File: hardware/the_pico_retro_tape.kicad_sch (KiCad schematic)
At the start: 1 part, among them U1 Pico

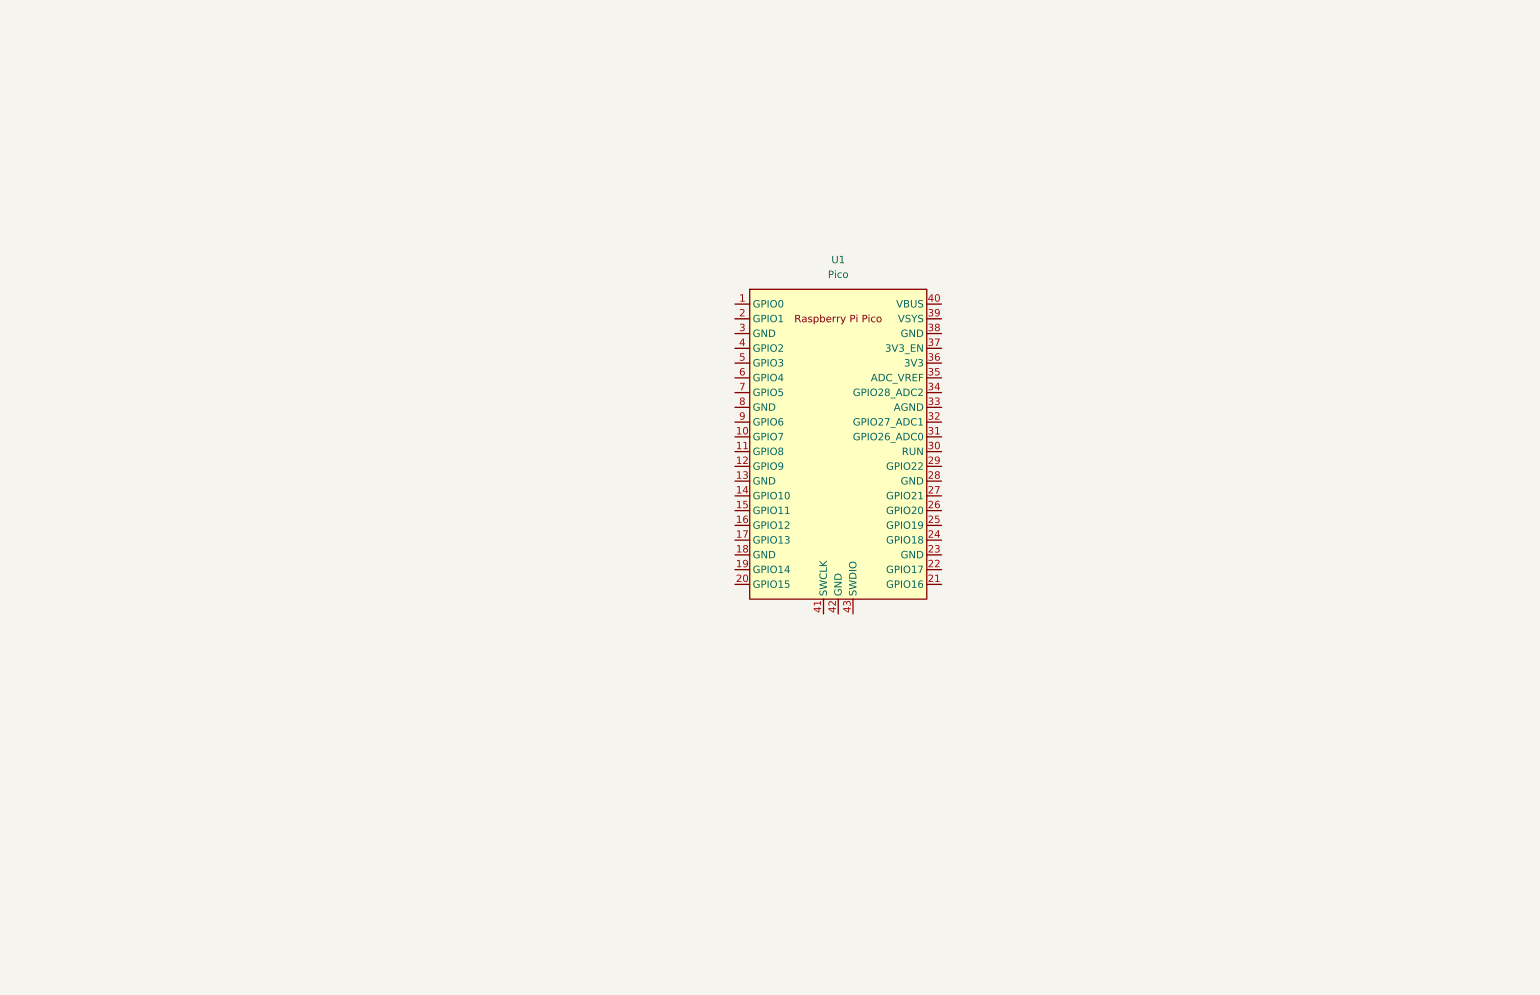
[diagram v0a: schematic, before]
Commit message: update schematic
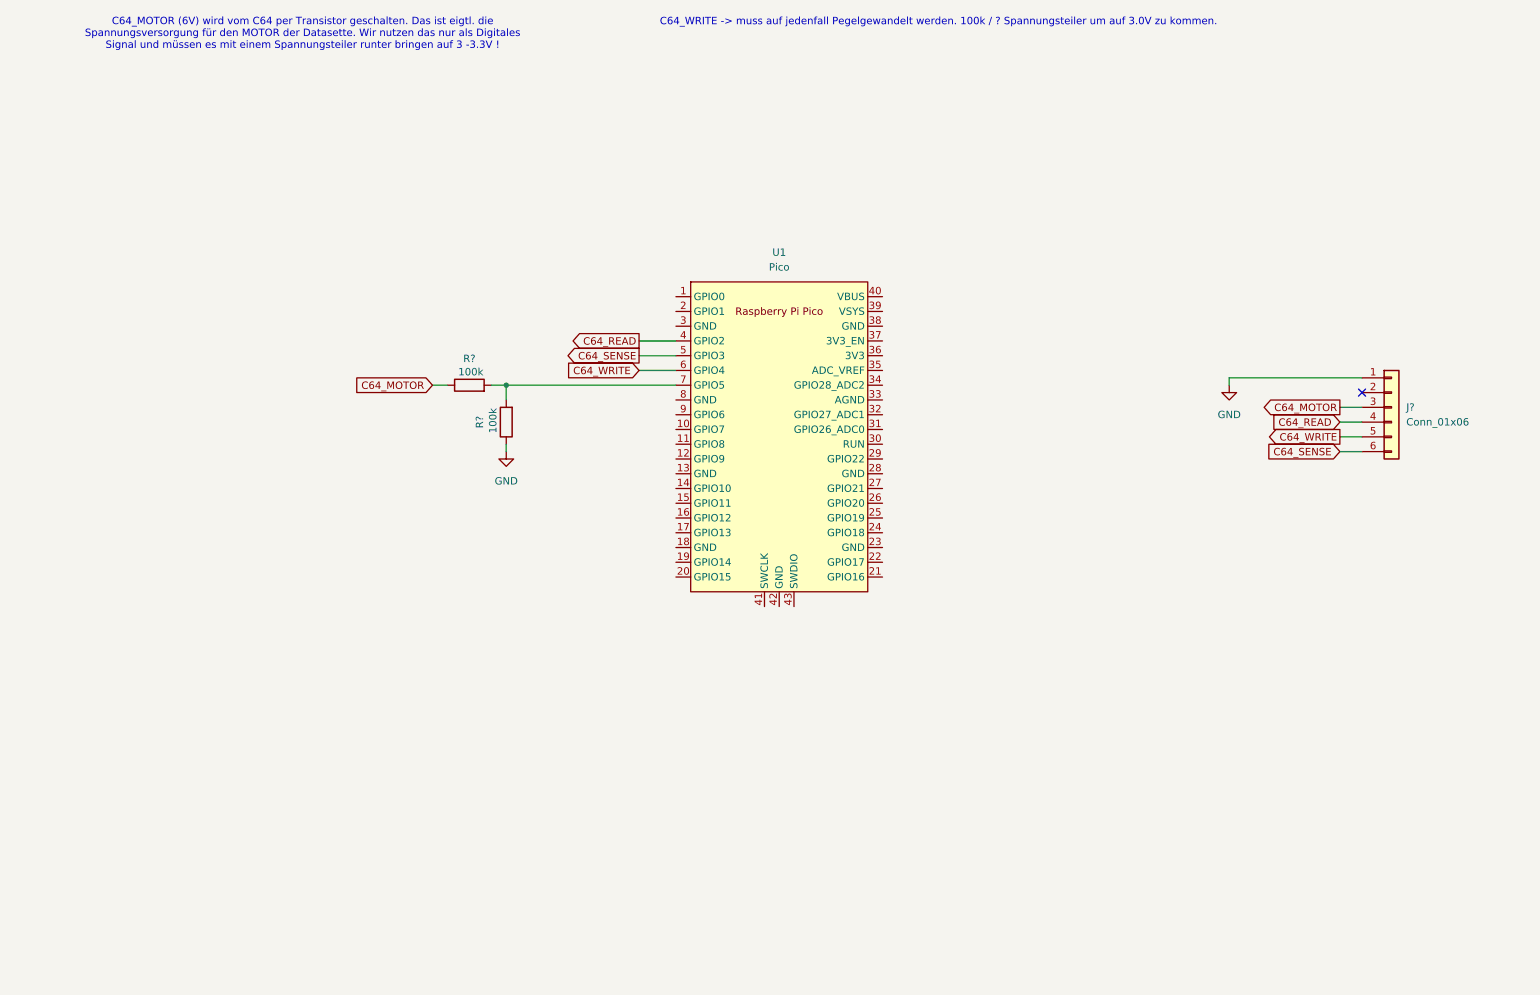
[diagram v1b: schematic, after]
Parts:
- added J?: Conn_01x06, symbol Connector_Generic:Conn_01x06
- added R? (x2): 100k, symbol Device:R
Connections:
- net C64_READ: now reaches U1.4 (GPIO2)
- net C64_READ: now also J?.4 (Pin_4)
- net C64_SENSE: now reaches U1.5 (GPIO3)
- net C64_SENSE: now also J?.6 (Pin_6)
- net C64_WRITE: now reaches U1.6 (GPIO4)
- net C64_WRITE: now also J?.5 (Pin_5)
- net at U1.7 (GPIO5): now also R?.2, R?.2
- new net C64_MOTOR: J?.3 (Pin_3), R?.1
- new net GND: J?.1 (Pin_1), R?.1
- no-connect marks 0 -> 1
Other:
- note added: "C64_MOTOR (6V) wird vom C64 per Transistor geschalten. Das ist eigtl. die Spannungsversorgung für den MOTOR der Datasette. Wir nutzen das nur als Digitales Signal und müssen es mit einem Spannungsteiler runter bringen auf 3 -3.3V !"
- note added: "C64_WRITE -> muss auf jedenfall Pegelgewandelt werden. 100k / ? Spannungsteiler um auf 3.0V zu kommen."
- moved on the sheet: U1

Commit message: schematic: added the sd card modul
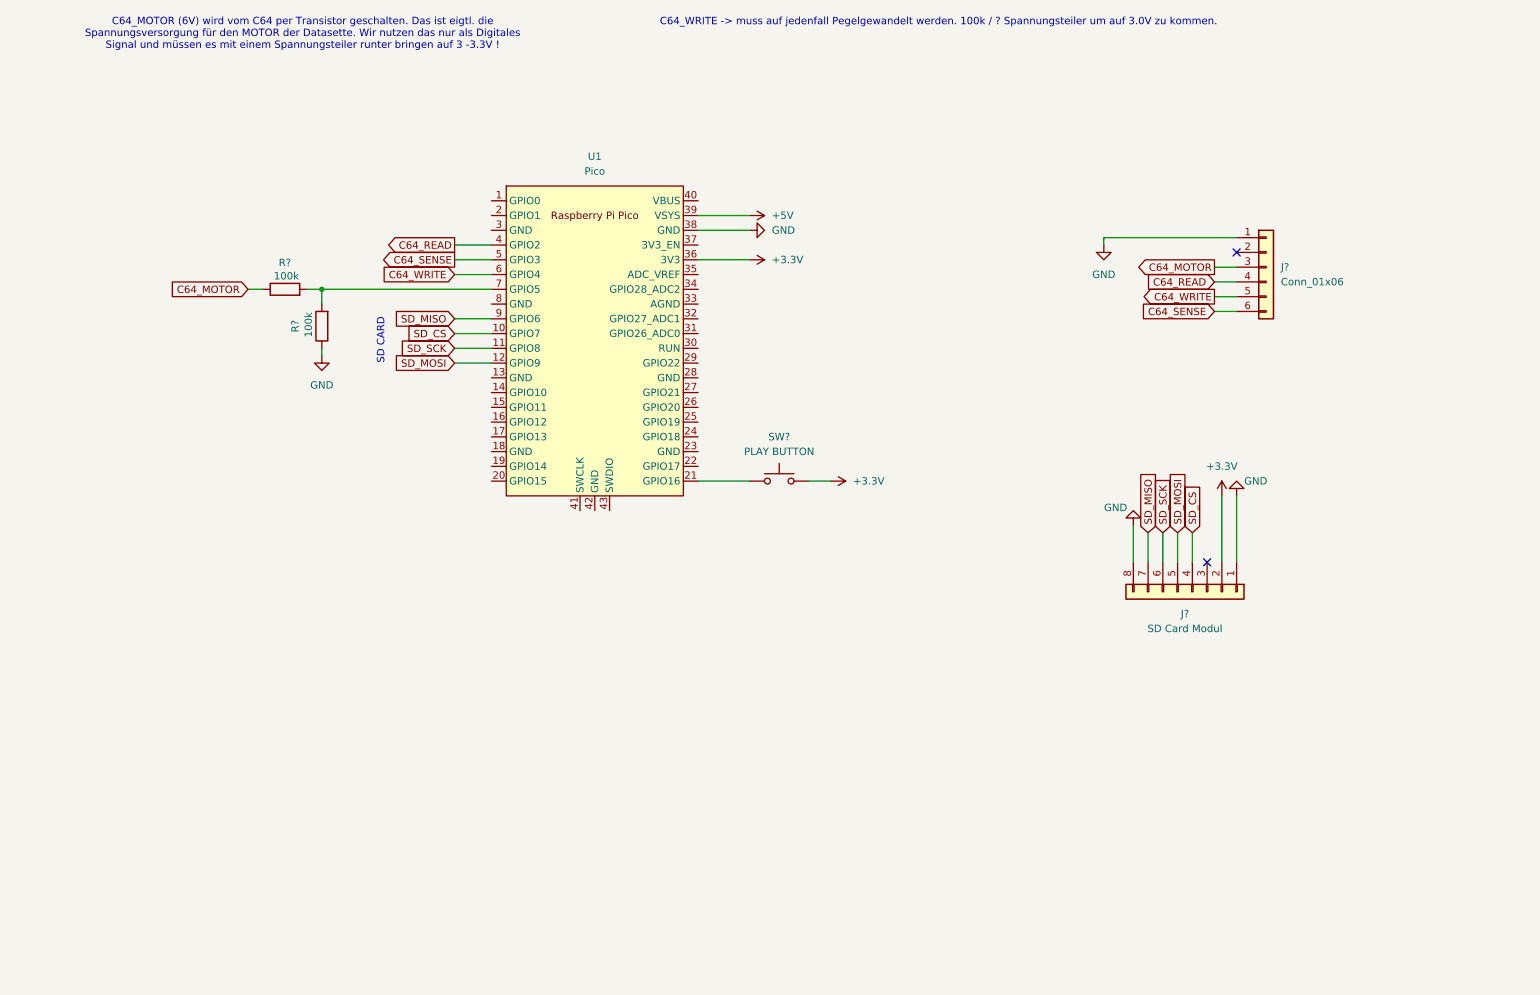
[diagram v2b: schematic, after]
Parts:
- added J?: SD Card Modul, symbol Connector_Generic:Conn_01x08
- added SW?: PLAY BUTTON, symbol Switch:SW_Push
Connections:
- net GND: now also U1.38 (GND), J?.1 (Pin_1), J?.8 (Pin_8)
- net SD_CS: now reaches U1.10 (GPIO7)
- net SD_CS: now also J?.4 (Pin_4)
- net SD_SCK: now reaches U1.11 (GPIO8)
- net SD_SCK: now also J?.6 (Pin_6)
- net SD_MOSI: now reaches U1.12 (GPIO9)
- net SD_MOSI: now also J?.5 (Pin_5)
- net at U1.21 (GPIO16): now also SW?.1
- net +3.3V: now reaches U1.36 (3V3)
- net +3.3V: now also J?.2 (Pin_2), SW?.2
- net +5V: now reaches U1.39 (VSYS)
- net SD_MISO: now reaches U1.9 (GPIO6)
- net SD_MISO: now also J?.7 (Pin_7)
- no-connect marks 1 -> 2
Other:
- note added: "SD CARD"
- moved on the sheet: J?, R?, U1

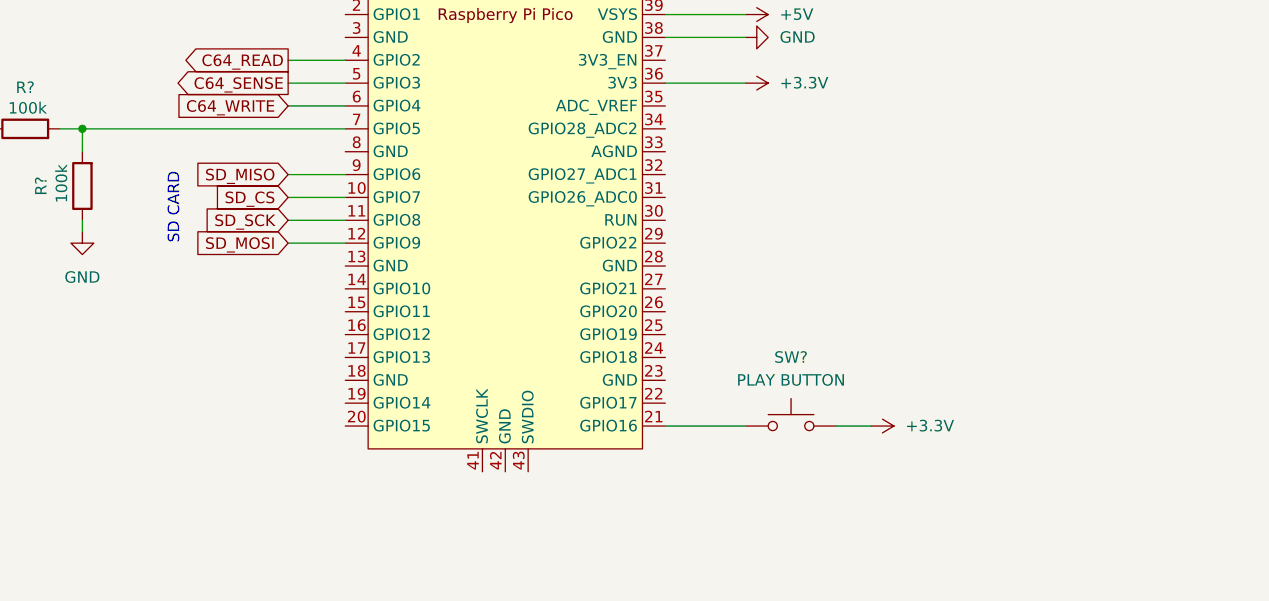
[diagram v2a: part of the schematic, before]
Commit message: hardware: changed gpios for sd card slot
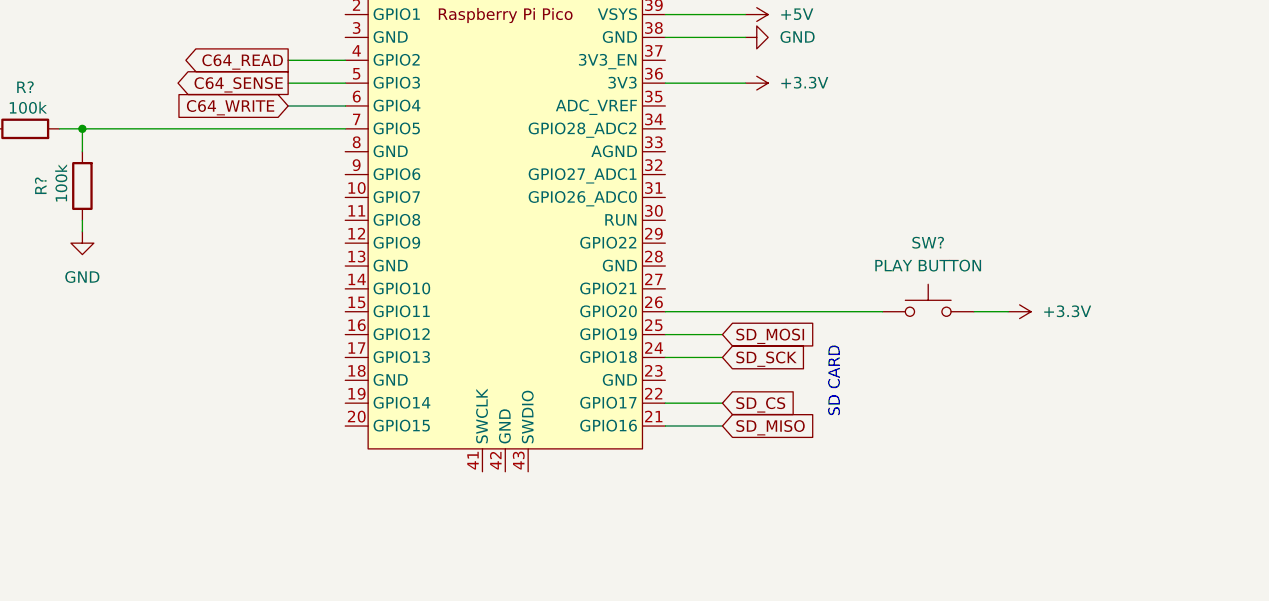
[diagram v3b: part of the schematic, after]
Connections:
- net SD_CS: now also U1.22 (GPIO17); no longer U1.10 (GPIO7)
- net SD_MISO: now also U1.21 (GPIO16); no longer U1.9 (GPIO6)
- net SD_MOSI: now also U1.25 (GPIO19); no longer U1.12 (GPIO9)
- net SD_SCK: now also U1.24 (GPIO18); no longer U1.11 (GPIO8)
- net at SW?.1: now also U1.26 (GPIO20); no longer U1.21 (GPIO16)
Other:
- moved on the sheet: SW?
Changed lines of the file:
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@@
+	(wire
+		(pts
+			(xy 124.46 83.82) (xy 148.59 83.82)
+		)
+		(stroke
+			(width 0)
+			(type default)
+		)
+	)
 	(wire
 		(pts
@@
 	(wire
 		(pts
-			(xy 82.55 71.12) (xy 88.9 71.12)
+			(xy 130.81 93.98) (xy 124.46 93.98)
 		)
 		(stroke
@@
 	(wire
 		(pts
-			(xy 82.55 76.2) (xy 88.9 76.2)
+			(xy 130.81 86.36) (xy 124.46 86.36)
 		)
 		(stroke
@@
 	(wire
 		(pts
-			(xy 82.55 68.58) (xy 88.9 68.58)
+			(xy 130.81 96.52) (xy 124.46 96.52)
 		)
 		(stroke
@@
 	(wire
 		(pts
-			(xy 124.46 96.52) (xy 133.35 96.52)
-		)
-		(stroke
-			(width 0)
-			(type default)
-		)
-	)
-	(wire
-		(pts
 			(xy 59.69 63.5) (xy 59.69 66.04)
 		)
@@
 	(wire
 		(pts
-			(xy 143.51 96.52) (xy 147.32 96.52)
+			(xy 158.75 83.82) (xy 162.56 83.82)
 		)
 		(stroke
@@
 	(wire
 		(pts
-			(xy 82.55 73.66) (xy 88.9 73.66)
+			(xy 130.81 88.9) (xy 124.46 88.9)
 		)
 		(stroke
@@
 	(text "SD CARD"
 		(exclude_from_sim no)
-		(at 69.85 72.39 90)
+		(at 143.256 91.694 90)
 		(effects
 			(font
@@
 	(global_label "SD_MOSI"
 		(shape input)
-		(at 82.55 76.2 180)
-		(fields_autoplaced yes)
-		(effects
-			(font
-				(size 1.27 1.27)
-			)
-			(justify right)
-		)
-		(property "Intersheetrefs" "${INTERSHEET_REFS}"
-			(at 71.5215 76.2 0)
-			(effects
-				(font
-					(size 1.27 1.27)
-				)
-				(justify right)
+		(at 130.81 86.36 0)
+		(fields_autoplaced yes)
+		(effects
+			(font
+				(size 1.27 1.27)
+			)
+			(justify left)
+		)
+		(property "Intersheetrefs" "${INTERSHEET_REFS}"
+			(at 141.8385 86.36 0)
+			(effects
+				(font
+					(size 1.27 1.27)
+				)
+				(justify left)
 				(hide yes)
 			)
@@
 	(global_label "SD_MISO"
 		(shape input)
-		(at 82.55 68.58 180)
-		(fields_autoplaced yes)
-		(effects
-			(font
-				(size 1.27 1.27)
-			)
-			(justify right)
-		)
-		(property "Intersheetrefs" "${INTERSHEET_REFS}"
-			(at 71.5215 68.58 0)
-			(effects
-				(font
-					(size 1.27 1.27)
-				)
-				(justify right)
+		(at 130.81 96.52 0)
+		(fields_autoplaced yes)
+		(effects
+			(font
+				(size 1.27 1.27)
+			)
+			(justify left)
+		)
+		(property "Intersheetrefs" "${INTERSHEET_REFS}"
+			(at 141.8385 96.52 0)
+			(effects
+				(font
+					(size 1.27 1.27)
+				)
+				(justify left)
 				(hide yes)
 			)
@@
 	(global_label "SD_SCK"
 		(shape input)
-		(at 82.55 73.66 180)
-		(fields_autoplaced yes)
-		(effects
-			(font
-				(size 1.27 1.27)
-			)
-			(justify right)
-		)
-		(property "Intersheetrefs" "${INTERSHEET_REFS}"
-			(at 72.3682 73.66 0)
-			(effects
-				(font
-					(size 1.27 1.27)
-				)
-				(justify right)
+		(at 130.81 88.9 0)
+		(fields_autoplaced yes)
+		(effects
+			(font
+				(size 1.27 1.27)
+			)
+			(justify left)
+		)
+		(property "Intersheetrefs" "${INTERSHEET_REFS}"
+			(at 140.9918 88.9 0)
+			(effects
+				(font
+					(size 1.27 1.27)
+				)
+				(justify left)
 				(hide yes)
 			)
@@
 	(global_label "SD_CS"
 		(shape input)
-		(at 82.55 71.12 180)
-		(fields_autoplaced yes)
-		(effects
-			(font
-				(size 1.27 1.27)
-			)
-			(justify right)
-		)
-		(property "Intersheetrefs" "${INTERSHEET_REFS}"
-			(at 73.6382 71.12 0)
-			(effects
-				(font
-					(size 1.27 1.27)
-				)
-				(justify right)
+		(at 130.81 93.98 0)
+		(fields_autoplaced yes)
+		(effects
+			(font
+				(size 1.27 1.27)
+			)
+			(justify left)
+		)
+		(property "Intersheetrefs" "${INTERSHEET_REFS}"
+			(at 139.7218 93.98 0)
+			(effects
+				(font
+					(size 1.27 1.27)
+				)
+				(justify left)
 				(hide yes)
 			)
@@
 	(symbol
 		(lib_id "Switch:SW_Push")
-		(at 138.43 96.52 0)
+		(at 153.67 83.82 0)
 		(unit 1)
 		(exclude_from_sim no)
@@
 		(fields_autoplaced yes)
 		(property "Reference" "SW?"
-			(at 138.43 88.9 0)
+			(at 153.67 76.2 0)
 			(effects
 				(font
@@
 		)
 		(property "Value" "PLAY BUTTON"
-			(at 138.43 91.44 0)
+			(at 153.67 78.74 0)
 			(effects
 				(font
@@
 		)
 		(property "Footprint" ""
-			(at 138.43 91.44 0)
+			(at 153.67 78.74 0)
 			(effects
 				(font
@@
 		)
 		(property "Datasheet" "~"
-			(at 138.43 91.44 0)
+			(at 153.67 78.74 0)
 			(effects
 				(font
@@
 		)
 		(property "Description" "Push button switch, generic, two pins"
-			(at 138.43 96.52 0)
+			(at 153.67 83.82 0)
 			(effects
 				(font
@@
 	(symbol
 		(lib_id "power:+3.3V")
-		(at 147.32 96.52 270)
+		(at 162.56 83.82 270)
 		(unit 1)
 		(exclude_from_sim no)
@@
 		(fields_autoplaced yes)
 		(property "Reference" "#PWR04"
-			(at 143.51 96.52 0)
+			(at 158.75 83.82 0)
 			(effects
 				(font
@@
 		)
 		(property "Value" "+3.3V"
-			(at 151.13 96.5199 90)
+			(at 166.37 83.8199 90)
 			(effects
 				(font
@@
 		)
 		(property "Footprint" ""
-			(at 147.32 96.52 0)
+			(at 162.56 83.82 0)
 			(effects
 				(font
@@
 		)
 		(property "Datasheet" ""
-			(at 147.32 96.52 0)
+			(at 162.56 83.82 0)
 			(effects
 				(font
@@
 		)
 		(property "Description" "Power symbol creates a global label with name \"+3.3V\""
-			(at 147.32 96.52 0)
-			(effects
-				(font
+			(at 162.56 83.82 0)
+			(effects
+				(font
